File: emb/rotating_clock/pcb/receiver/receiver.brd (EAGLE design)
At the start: 100 x 80 mm, 23 parts, among them IC1 A1321LH, IC2 A1321LH, IC3 A1321LH, IC4 LM358D, IC5 LM358D

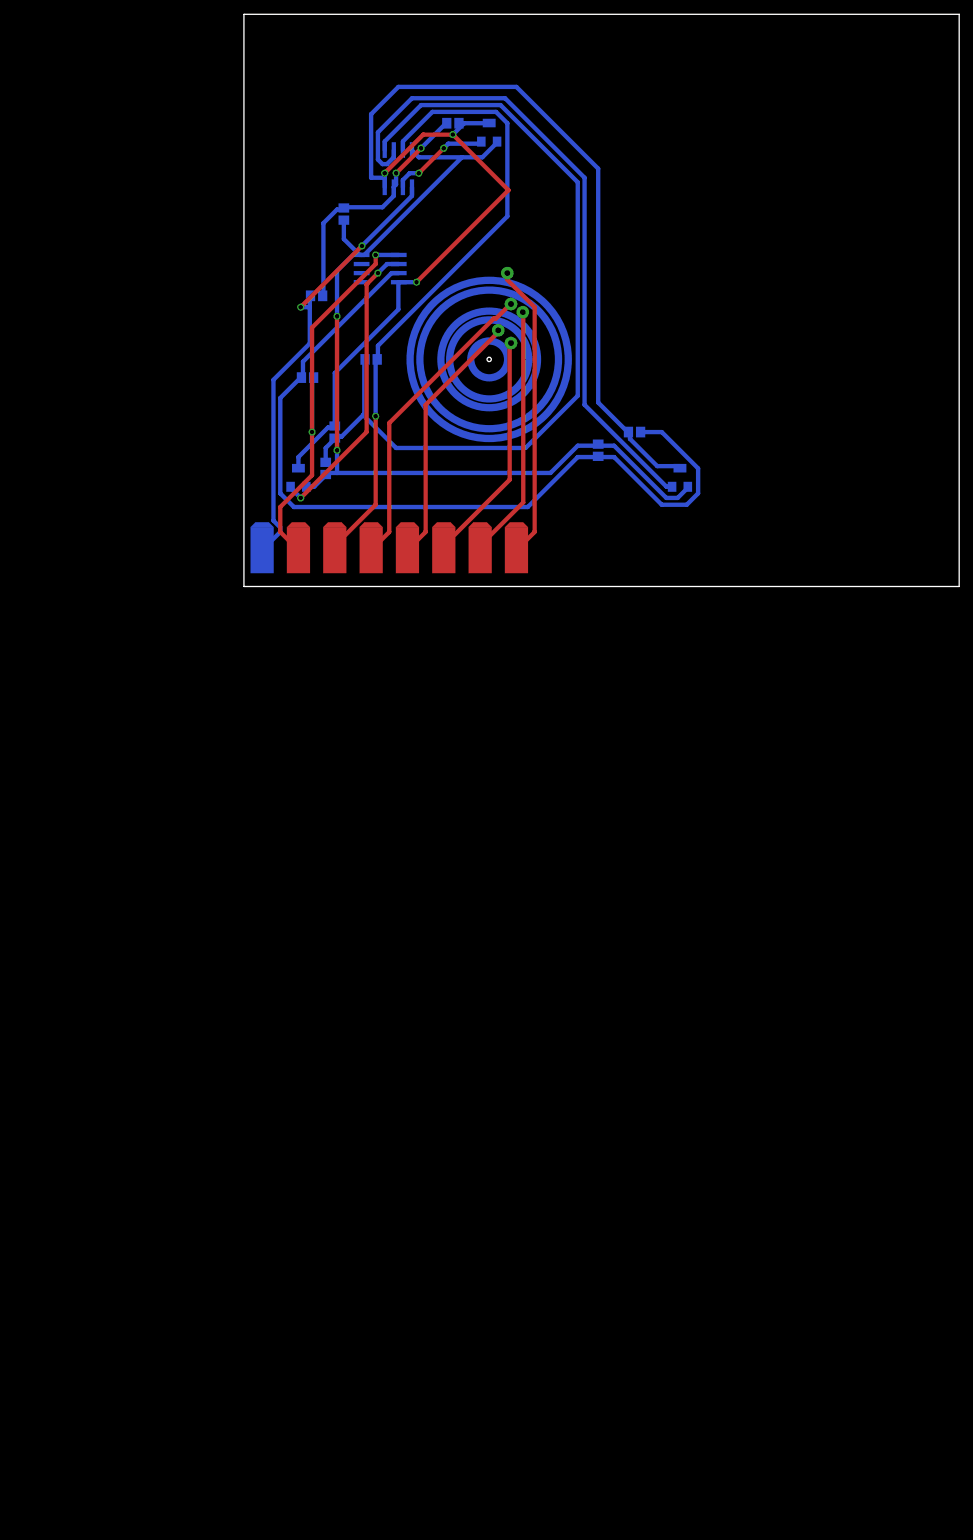
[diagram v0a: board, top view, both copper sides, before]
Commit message: Updated bot board schematic
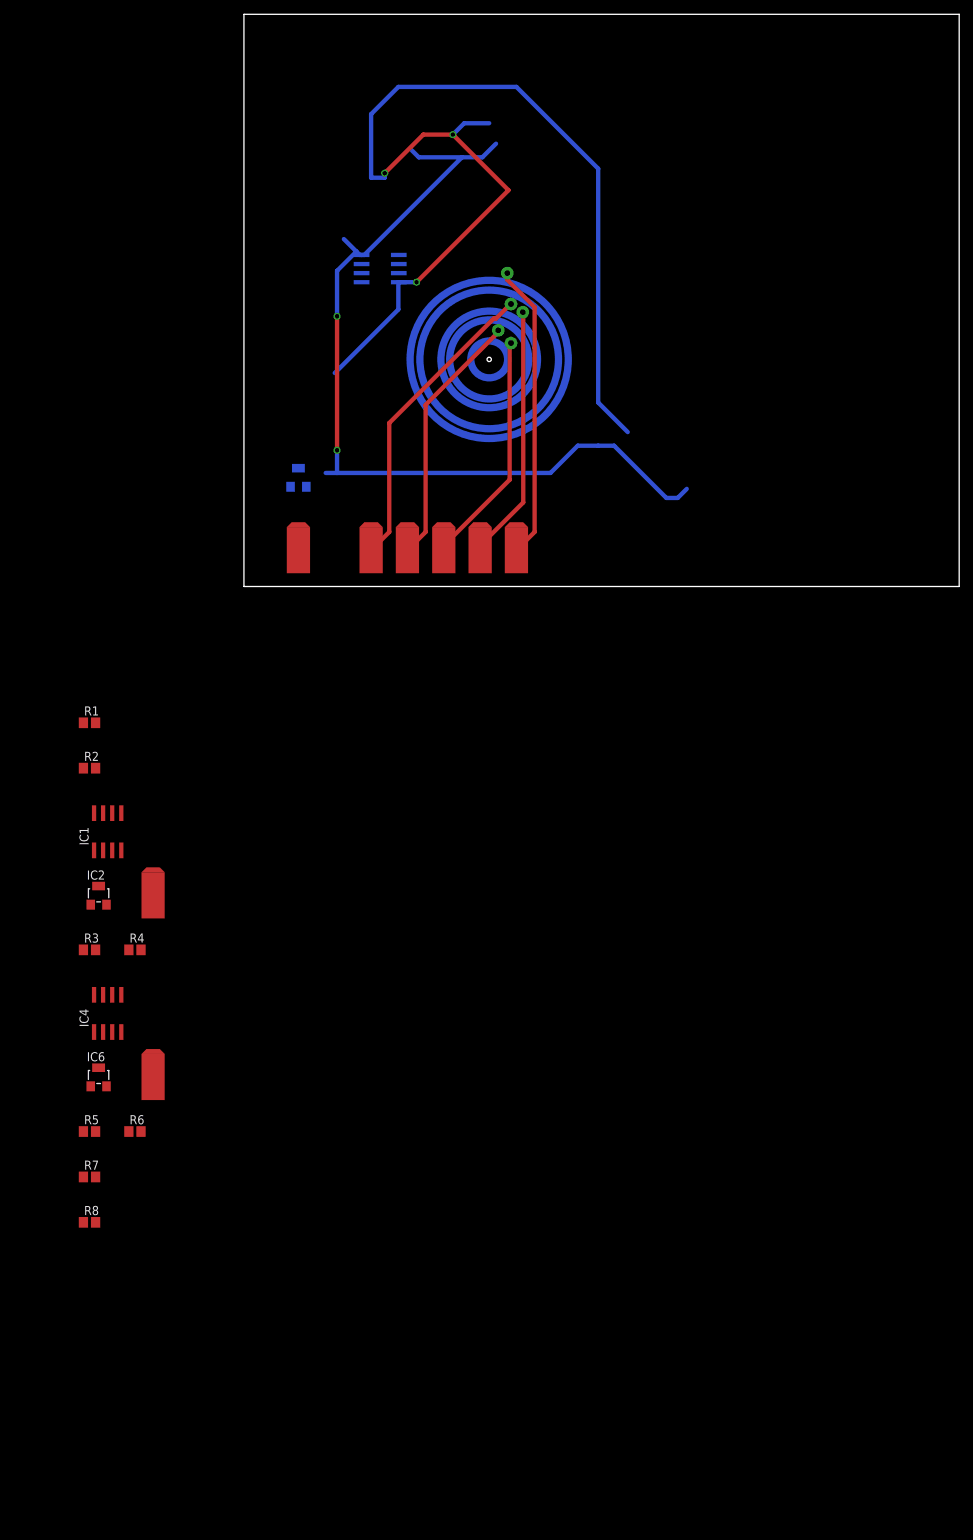
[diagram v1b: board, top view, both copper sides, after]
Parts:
- removed R9: (no value), resistor:R0805
- added IC6: A1321LH, allegro:SOT23-W
- IC1: value A1321LH -> LM358D; device allegro:SOT23-W -> linear:SO08
- R1, R2, R3, R4, R5, R6: value (none) -> 200K
- R7: value (none) -> 3.75k
- R8: value (none) -> 1.25k
- moved R3 126.2 mm to (-21.6, -50.8), flipped to the top
- moved IC4 124.9 mm to (-19.1, -59.7), flipped to the top
- moved R7 120.9 mm to (-21.6, -82.5), flipped to the top, turned to 0 degrees
- moved R6 120.2 mm to (-15.2, -76.2), flipped to the top, turned to 0 degrees
- moved R5 118.9 mm to (-21.6, -76.2), flipped to the top, turned to 0 degrees
- moved IC1 111.4 mm to (-19.1, -34.3), flipped to the top
- moved R8 110.5 mm to (-21.6, -88.9), flipped to the top, turned to 0 degrees
- moved IC2 100.1 mm to (-20.3, -43.2), flipped to the top
- moved R2 85.2 mm to (-21.6, -25.4), flipped to the top, turned to 0 degrees
- moved R4 83.6 mm to (-15.2, -50.8), flipped to the top, turned to 0 degrees
- moved U$4 75.2 mm to (-12.7, -68.6), flipped to the top
- moved R1 67.6 mm to (-21.6, -19.1), flipped to the top
- moved U$3 54.5 mm to (-12.7, -43.2)
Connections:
- net N$3 renamed VCC
- removed net +3V3: IC1.1, IC2.1, IC3.1, IC4.8, IC5.8, R2.1, R5.1, R8.1
- removed net N$2: IC4.1, R1.2, U$4.P$1
- new net 3.75V: IC5.2, R7.1, R8.2
- new net 5V: IC1.8, IC2.1, IC3.1, IC4.8, IC5.8, IC6.1, R7.2
- new net N$3: IC1.1, R4.2, U$3.P$1
- new net R20: IC1.3, R3.2, R4.1
- net GND: now also IC1.4, IC6.3, R8.1; no longer IC1.3, R3.1, R6.1, R9.1
- net N$1: now also IC2.2, R3.1; no longer IC4.3, R1.1, R2.2, R3.2
- net N$4: now also IC3.2, R1.1; no longer IC5.3, R4.1, R5.2, R6.2
- net N$5: now also IC5.3, R1.2, R2.1; no longer IC5.1, R4.2, U$2.P$1
- net N$6: now also IC5.1, R2.2, U$2.P$1; no longer IC3.2, IC5.2
- net N$7: now also IC6.2, R5.1; no longer IC4.5, R7.1, R8.2, R9.2
- net N$8: now also IC4.3, R5.2, R6.1; no longer IC4.7, R7.2, U$3.P$1
- net N$9: now also IC4.1, R6.2, U$4.P$1; no longer IC2.2, IC4.6
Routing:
- net +3V3: track 131.0 -> 0.00 mm, vias 2 -> 0
- net 5V: track 0.00 -> 123.7 mm, vias 0 -> 2
- net N$4: track 117.7 -> 0.00 mm
- net N$7: track 116.8 -> 0.00 mm
- net N$9: track 91.9 -> 0.00 mm
- net N$8: track 88.1 -> 0.00 mm, vias 1 -> 0
- net N$2: track 63.7 -> 0.00 mm, vias 2 -> 0
- net N$5: track 58.9 -> 0.00 mm, vias 2 -> 0
- net N$6: track 41.5 -> 0.00 mm, vias 2 -> 0
- net N$1: track 35.2 -> 0.00 mm, vias 2 -> 0
- net GND: track 181.8 -> 153.6 mm
- net VCC: track 14.2 -> 0.00 mm, vias 2 -> 0

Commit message: Report stuff
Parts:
- R2, R4, R6: value 200K -> 1M
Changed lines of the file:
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@@
 <element name="U$9" library="slip_ring" package="CONNECTOR" value="" x="27.94" y="5.08"/>
 <element name="R1" library="resistor" package="R0805" value="200K" x="-21.59" y="-19.05"/>
-<element name="R2" library="resistor" package="R0805" value="200K" x="-21.59" y="-25.4"/>
+<element name="R2" library="resistor" package="R0805" value="1M" x="-21.59" y="-25.4"/>
 <element name="IC1" library="linear" package="SO08" value="LM358D" x="-19.05" y="-34.29"/>
 <element name="IC2" library="allegro" package="SOT23-W" value="A1321LH" x="-20.32" y="-43.18">
@@
 <element name="U$3" library="slip_ring" package="CONNECTOR" value="" x="-12.7" y="-43.18"/>
 <element name="R3" library="resistor" package="R0805" value="200K" x="-21.59" y="-50.8"/>
-<element name="R4" library="resistor" package="R0805" value="200K" x="-15.24" y="-50.8"/>
+<element name="R4" library="resistor" package="R0805" value="1M" x="-15.24" y="-50.8"/>
 <element name="IC4" library="linear" package="SO08" value="LM358D" x="-19.05" y="-59.69"/>
 <element name="IC6" library="allegro" package="SOT23-W" value="A1321LH" x="-20.32" y="-68.58">
@@
 <element name="U$4" library="slip_ring" package="CONNECTOR" value="" x="-12.7" y="-68.58"/>
 <element name="R5" library="resistor" package="R0805" value="200K" x="-21.59" y="-76.2"/>
-<element name="R6" library="resistor" package="R0805" value="200K" x="-15.24" y="-76.2"/>
+<element name="R6" library="resistor" package="R0805" value="1M" x="-15.24" y="-76.2"/>
 <element name="R7" library="resistor" package="R0805" value="3.75k" x="-21.59" y="-82.55"/>
 <element name="R8" library="resistor" package="R0805" value="1.25k" x="-21.59" y="-88.9"/>

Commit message: Report stuff
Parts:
- added PWM: PWM, slip_ring:CONNECTOR
- added Q1: NTD5867NL, adafruit:TO220V
- added Q2, Q3, Q4: BSS138, SparkFun:SOT23-3
- added R10, R11, R12, R13, R14, R9: 10K, SparkFun:0603-RES
- moved U$2 125.3 mm to (-30.5, -114.3)
- moved U$3 84.4 mm to (-30.5, -125.7)
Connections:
- removed net N$3: IC1.1, R4.2, U$3.P$1
- removed net N$6: IC5.1, R2.2, U$2.P$1
- removed net N$9: IC4.1, R6.2, U$4.P$1
- new net 1: IC5.1, R2.2
- new net 2: IC1.1, R4.2
- new net 3: IC4.1, R6.2
- new net HV: R10.1, R12.1, R14.1
- new net HV1: Q2.3, R10.2, U$4.P$1
- new net HV2: Q3.3, R12.2, U$2.P$1
- new net HV3: Q4.3, R14.2, U$3.P$1
- new net N$2: PWM.P$1
- new net OUT1: Q2.2, R9.2
- new net OUT2: Q3.2, R11.2
- new net OUT3: Q4.2, R13.2
- net GND: now also Q1.3
- net VCC: now also Q1.2, Q2.1, Q3.1, Q4.1, R11.1, R13.1, R9.1

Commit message: Reportstuff
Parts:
- Q2, Q3, Q4: value BSS138 -> NDT5867NLT4G
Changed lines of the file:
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@@
 <element name="Q1" library="adafruit" package="TO220V" value="NTD5867NL" x="-17.78" y="-92.71"/>
 <element name="PWM" library="slip_ring" package="CONNECTOR" value="PWM" x="-30.48" y="-96.52"/>
-<element name="Q2" library="SparkFun" package="SOT23-3" value="BSS138" x="-30.48" y="-104.14"/>
+<element name="Q2" library="SparkFun" package="SOT23-3" value="NDT5867NLT4G" x="-30.48" y="-104.14"/>
 <element name="R9" library="SparkFun" package="0603-RES" value="10K" x="-26.67" y="-102.87"/>
 <element name="R10" library="SparkFun" package="0603-RES" value="10K" x="-30.48" y="-107.95"/>
 <element name="U$2" library="slip_ring" package="CONNECTOR" value="" x="-30.48" y="-114.3"/>
-<element name="Q3" library="SparkFun" package="SOT23-3" value="BSS138" x="-26.67" y="-113.03"/>
+<element name="Q3" library="SparkFun" package="SOT23-3" value="NDT5867NLT4G" x="-26.67" y="-113.03"/>
 <element name="R11" library="SparkFun" package="0603-RES" value="10K" x="-30.48" y="-119.38"/>
 <element name="R12" library="SparkFun" package="0603-RES" value="10K" x="-26.67" y="-119.38"/>
 <element name="U$3" library="slip_ring" package="CONNECTOR" value="" x="-30.48" y="-125.73"/>
-<element name="Q4" library="SparkFun" package="SOT23-3" value="BSS138" x="-26.67" y="-124.46"/>
+<element name="Q4" library="SparkFun" package="SOT23-3" value="NDT5867NLT4G" x="-26.67" y="-124.46"/>
 <element name="R13" library="SparkFun" package="0603-RES" value="10K" x="-30.48" y="-130.81"/>
 <element name="R14" library="SparkFun" package="0603-RES" value="10K" x="-26.67" y="-130.81"/>
